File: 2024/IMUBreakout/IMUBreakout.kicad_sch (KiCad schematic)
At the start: 5 parts, among them J1 SM06B-GHS-TB_LF__SN_, SW1 SW_Push, U1 BNO085

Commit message: Finished V1 Schematic
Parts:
- added R2, R3, R4: 220, symbol Device:R_US
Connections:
- net  SA0/H_MOSI: now also U1.17 (SA0/H_MOSI)
- net +3.3V: now also R2.1, R3.1, R4.1
- net H_CSN: now also U1.18 (H_CSN)
- net H_SDA/H_MISO: now also U1.20 (H_SDA/H_MISO/TX)
- net SCK: now also U1.19 (H_SCL/SCK/RX)
- net at U1.4 (BOOTN): now also R2.2
- net at U1.5 (PS1): now also R3.2
- net at U1.6 (PS0/WAKE): now also R4.2
- no-connect marks 0 -> 6

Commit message: imported symbols to PCB editor
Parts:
- C1: footprint (none) -> Capacitor_SMD:C_0603_1608Metric
- J1: footprint SM06B-GHS-TB_LF__SN_:JST_SM06B-GHS-TB_LF__SN_ -> IMUBreakoutFootprint:JST_SM06B-GHS-TB_LF__SN_
- R1, R2, R3, R4: footprint (none) -> Resistor_SMD:R_0603_1608Metric
- SW1: footprint (none) -> Button_Switch_SMD:SW_Push_1P1T_NO_6x6mm_H9.5mm
- U1: footprint LGA-28_CEV -> IMUBreakoutFootprint:LGA-28_CEV
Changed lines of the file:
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@@
 			)
 		)
-		(property "Footprint" ""
+		(property "Footprint" "Capacitor_SMD:C_0603_1608Metric"
 			(at 125.73 76.5048 0)
 			(effects
@@
 			)
 		)
-		(property "Footprint" ""
+		(property "Footprint" "Resistor_SMD:R_0603_1608Metric"
 			(at 105.664 66.294 90)
 			(effects
@@
 			)
 		)
-		(property "Footprint" "SM06B-GHS-TB_LF__SN_:JST_SM06B-GHS-TB_LF__SN_"
+		(property "Footprint" "IMUBreakoutFootprint:JST_SM06B-GHS-TB_LF__SN_"
 			(at 144.78 120.65 0)
 			(effects
@@
 			)
 		)
-		(property "Footprint" "LGA-28_CEV"
+		(property "Footprint" "IMUBreakoutFootprint:LGA-28_CEV"
 			(at 130.81 57.15 0)
 			(effects
@@
 			)
 		)
-		(property "Footprint" ""
+		(property "Footprint" "Resistor_SMD:R_0603_1608Metric"
 			(at 118.364 63.754 90)
 			(effects
@@
 			)
 		)
-		(property "Footprint" ""
+		(property "Footprint" "Resistor_SMD:R_0603_1608Metric"
 			(at 94.234 68.834 90)
 			(effects
@@
 			)
 		)
-		(property "Footprint" ""
+		(property "Footprint" "Resistor_SMD:R_0603_1608Metric"
 			(at 91.694 81.534 90)
 			(effects
@@
 			)
 		)
-		(property "Footprint" ""
+		(property "Footprint" "Button_Switch_SMD:SW_Push_1P1T_NO_6x6mm_H9.5mm"
 			(at 92.71 87.63 0)
 			(effects

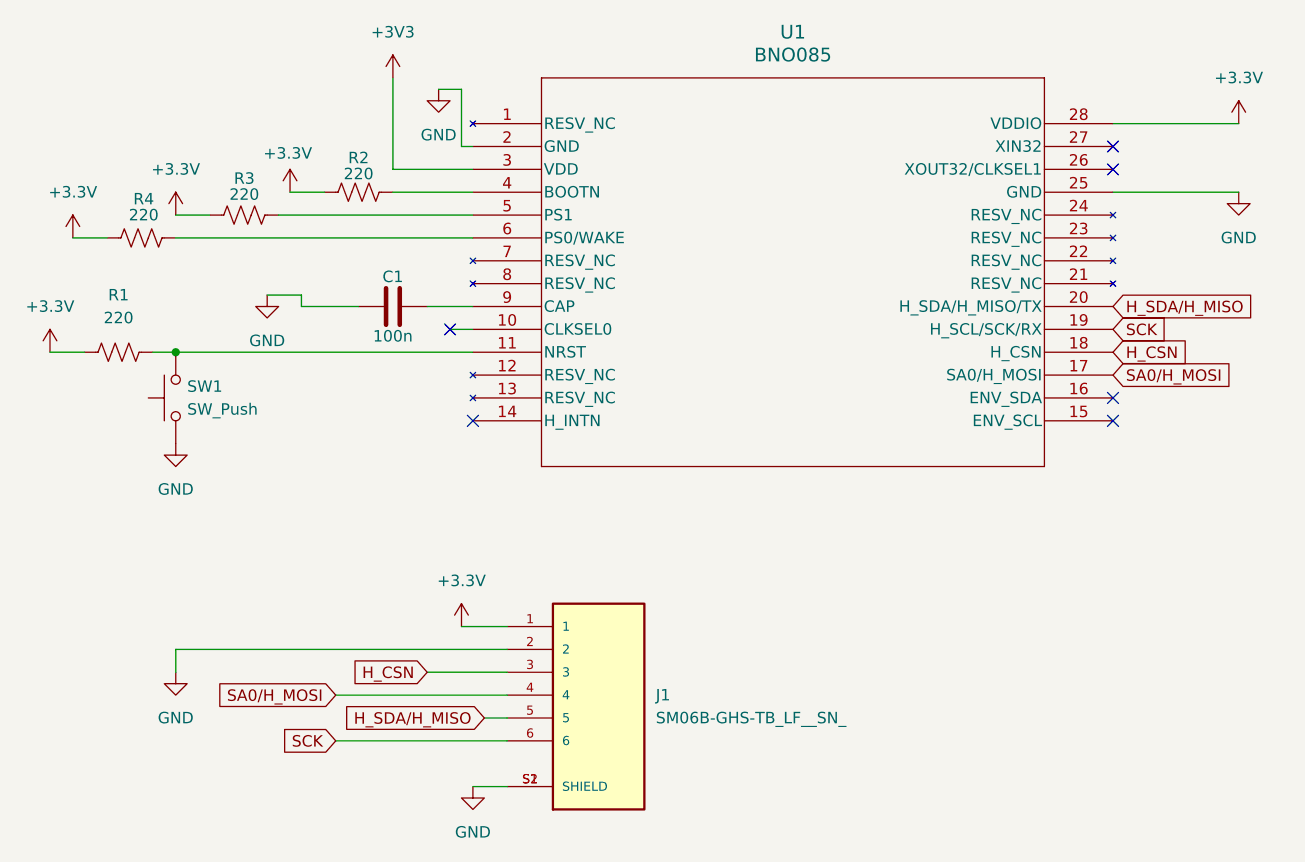
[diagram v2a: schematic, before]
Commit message: Connected all pins on IMU breakout PBC editor
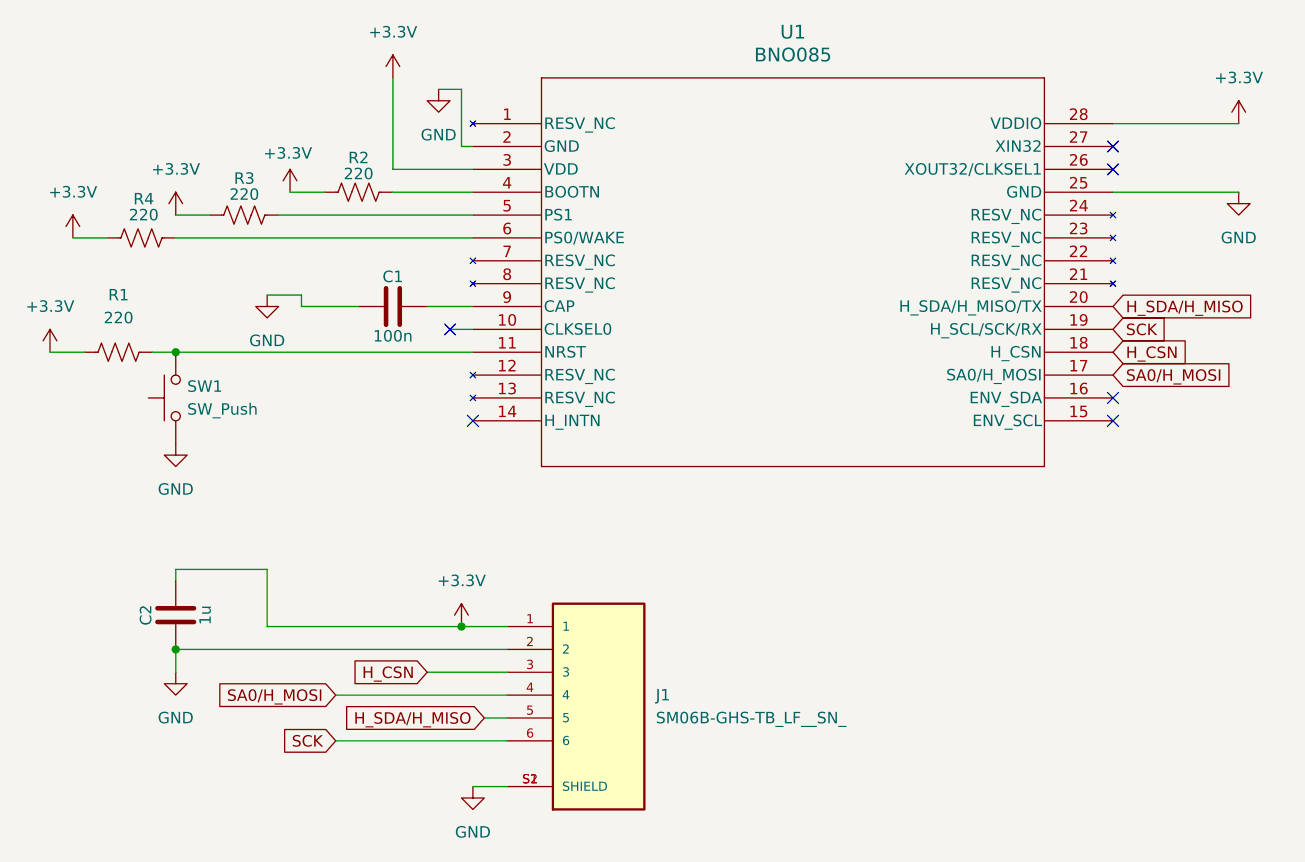
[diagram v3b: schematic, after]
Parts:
- added C2: 1u, Capacitor_SMD:C_0603_1608Metric, symbol Device:C
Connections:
- net +3V3 is gone; now on net +3.3V: U1.3 (VDD)
- net +3.3V: now also C2.2
- net GND: now also C2.1
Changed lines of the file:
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@@
 	(paper "A4")
+	(junction
+		(at 129.54 113.03)
+		(diameter 0)
+		(color 0 0 0 0)
+	)
+	(junction
+		(at 97.79 115.57)
+		(diameter 0)
+		(color 0 0 0 0)
+	)
 	(junction
 		(at 97.79 82.55)
@@
 	(wire
 		(pts
+			(xy 107.95 106.68) (xy 97.79 106.68)
+		)
+		(stroke
+			(width 0)
+			(type default)
+		)
+	)
+	(wire
+		(pts
 			(xy 110.49 64.77) (xy 114.3 64.77)
 		)
@@
 	(wire
 		(pts
+			(xy 97.79 106.68) (xy 97.79 107.95)
+		)
+		(stroke
+			(width 0)
+			(type default)
+		)
+	)
+	(wire
+		(pts
 			(xy 130.81 62.23) (xy 121.92 62.23)
 		)
@@
 	(wire
 		(pts
+			(xy 129.54 113.03) (xy 107.95 113.03)
+		)
+		(stroke
+			(width 0)
+			(type default)
+		)
+	)
+	(wire
+		(pts
 			(xy 127 53.34) (xy 129.54 53.34)
 		)
@@
 		(pts
 			(xy 115.57 125.73) (xy 134.62 125.73)
+		)
+		(stroke
+			(width 0)
+			(type default)
+		)
+	)
+	(wire
+		(pts
+			(xy 107.95 113.03) (xy 107.95 106.68)
 		)
 		(stroke
@@
 			)
 		)
-		(property "Value" "+3V3"
+		(property "Value" "+3.3V"
 			(at 121.92 46.99 0)
 			(effects
@@
 					(unit 1)
 				)
+			)
+		)
+	)
+	(symbol
+		(lib_id "Device:C")
+		(at 97.79 111.76 180)
+		(unit 1)
+		(exclude_from_sim no)
+		(in_bom yes)
+		(on_board yes)
+		(dnp no)
+		(property "Reference" "C2"
+			(at 94.488 111.76 90)
+			(effects
+				(font
+					(size 1.27 1.27)
+				)
+			)
+		)
+		(property "Value" "1u"
+			(at 101.092 111.76 90)
+			(effects
+				(font
+					(size 1.27 1.27)
+				)
+			)
+		)
+		(property "Footprint" "Capacitor_SMD:C_0603_1608Metric"
+			(at 96.8248 107.95 0)
+			(effects
+				(font
+					(size 1.27 1.27)
+				)
+				(hide yes)
+			)
+		)
+		(property "Datasheet" "~"
+			(at 97.79 111.76 0)
+			(effects
+				(font
+					(size 1.27 1.27)
+				)
+				(hide yes)
+			)
+		)
+		(property "Description" "Unpolarized capacitor"
+			(at 97.79 111.76 0)
+			(effects
+				(font
+					(size 1.27 1.27)
+				)
+				(hide yes)
+			)
+		)
+		(pin "1"
+		)
+		(pin "2"
+		)
+		(instances
+			(project "IMUBreakout"
+				(path "/bd538555-8bfc-451a-bd9d-2f650df5d8c2"
+					(reference "C2")
+					(unit 1)
+				)
